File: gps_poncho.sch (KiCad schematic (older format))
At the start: 2 parts

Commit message: Se completa esquematico
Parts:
- removed J?: Micro_SD_Card_Det, symbol Micro_SD_Card_Det
- added D1: LED, symbol LED
- added J1: Micro_SD_Card, symbol Micro_SD_Card
- added R1: 1K, symbol R
- added U11: SE868-A, symbol SE868-A
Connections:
- net labels added: SPI_MOSI
- wire segments 51 -> 97
- no-connect marks 48 -> 65
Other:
- note removed: "Borrar si no se quiere \nconexiones entre ambos \nconectores"
- note removed: "Este diseño puede copiarse para iniciar un poncho simple. \n1) Copiar toda la carpeta "Basico" , renombrando \n la misma al nombre del poncho.\n2) Renombrar los archivos "basico.xxx" manteniendo \n las extensiones pero cambiando a un nombre \n descriptivo del poncho. Evitar acentos, espacios y \n caracteres ascii esxtendidos."
- note removed: "Luego de abrir el nuevo proyecto:\n1)Editar datos del rótulo.\n2)Editar los archivos del subdirectorio "doc".\n2.1) Agregarse en el archivo de licencia.\n2.2) Colocar info mínima del Poncho en el LEEME.txt\n2.3) Colocar info mínima en el CAMBIOS.txt"
- note removed: "http://www.proyecto-ciaa.com.ar/"
- moved on the sheet: XA101A, XA101B

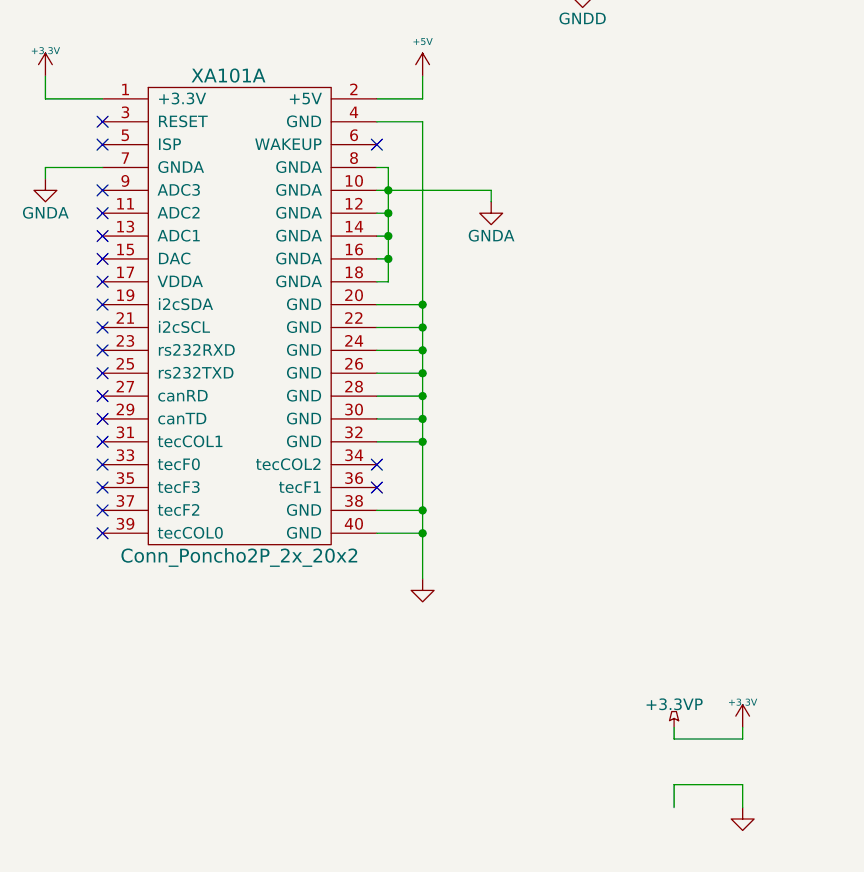
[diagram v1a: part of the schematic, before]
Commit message: Simplifico conexiones de los conectores laterales
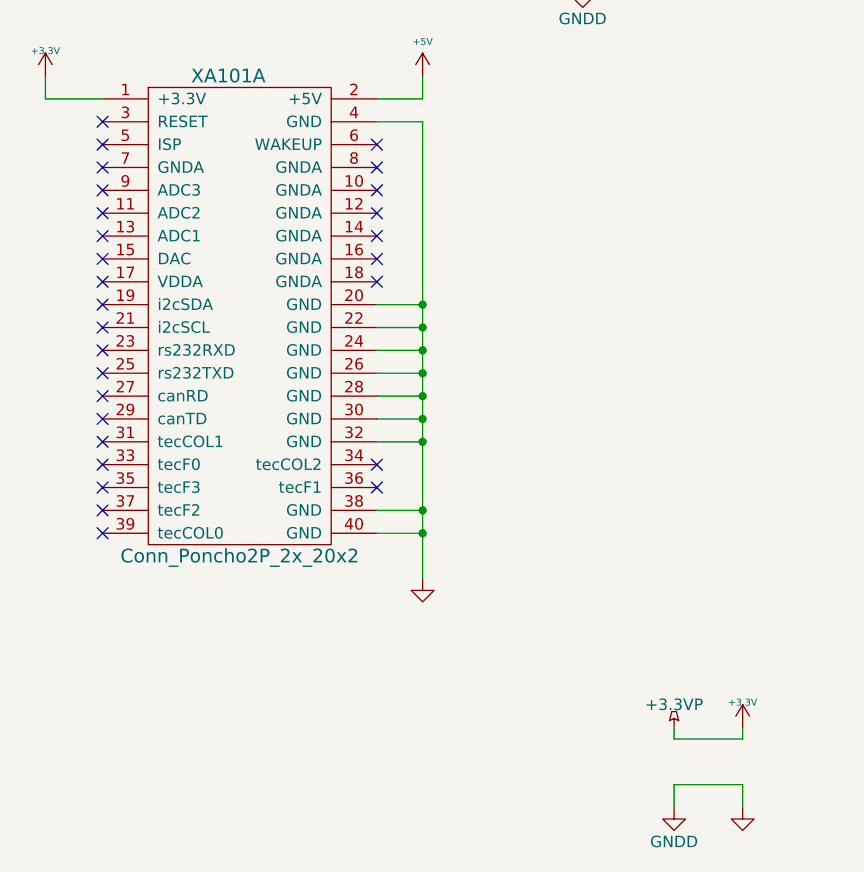
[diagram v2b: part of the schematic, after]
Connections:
- net GNDD is gone; now on net GND: D1.1 (K), J1.6 (VSS), J1.9 (SHIELD), U11.18 (RES), U11.23 (RX1), U11.24 (NC), U11.27 (NC), U11.3 (RES), U11.30 (SPI_MISO), XA101.43 (GND), XA101.45 (GND), XA101.47 (GND), XA101.51 (GND), XA101.53 (GND), XA101.57 (GND), XA101.59 (GND), XA101.65 (GND), XA101.67 (GND), XA101.77 (GND), XA101.79 (GND)
- removed net GNDA: XA101.10 (GNDA), XA101.12 (GNDA), XA101.14 (GNDA), XA101.16 (GNDA), XA101.18 (GNDA), XA101.7 (GNDA), XA101.8 (GNDA)
- no-connect marks 65 -> 72
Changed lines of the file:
@@
-$Comp
-L Conn_Poncho2P_2x_20x2 XA101
-U 1 1 57A7A0F8
-P 1700 4200
-F 0 "XA101" H 2000 4600 60  0000 C CNN
-F 1 "Conn_Poncho2P_2x_20x2" H 2050 2500 60  0000 C CNN
-F 2 "footprint:Conn_Poncho_SinBorde" H 1700 4200 60  0001 C CNN
-F 3 "" H 1700 4200 60  0000 C CNN
-F 4 "Harwin" H 1700 4200 60  0001 C CNN "Manf"
-F 5 "M50-3502042" H 1700 4200 60  0001 C CNN "Manf#"
-F 6 "952-1387-ND" H 1700 4200 60  0001 C CNN "Digikey#"
-	1    1700 4200
-	1    0    0    -1
-$EndComp
 $Comp
 L Conn_Poncho2P_2x_20x2 XA101
@@
 F 3 "" H 4250 7000 60  0000 C CNN
 	1    4250 7000
-	1    0    0    -1
-$EndComp
-$Comp
-L GNDA #PWR012
-U 1 1 57A7AE2B
-P 3150 4350
-F 0 "#PWR012" H 3150 4100 50  0001 C CNN
-F 1 "GNDA" H 3150 4200 50  0000 C CNN
-F 2 "" H 3150 4350 50  0000 C CNN
-F 3 "" H 3150 4350 50  0000 C CNN
-	1    3150 4350
-	1    0    0    -1
-$EndComp
-$Comp
-L GNDA #PWR013
-U 1 1 57A7AE5D
-P 1200 4250
-F 0 "#PWR013" H 1200 4000 50  0001 C CNN
-F 1 "GNDA" H 1200 4100 50  0000 C CNN
-F 2 "" H 1200 4250 50  0000 C CNN
-F 3 "" H 1200 4250 50  0000 C CNN
-	1    1200 4250
 	1    0    0    -1
 $EndComp
@@
 	4250 6900 4250 7000
 Wire Wire Line
-	1450 4200 1200 4200
-Wire Wire Line
-	1200 4200 1200 4250
-Wire Wire Line
-	2650 4200 2700 4200
-Wire Wire Line
-	2700 4200 2700 4700
-Wire Wire Line
-	2700 4700 2650 4700
-Wire Wire Line
-	2650 4600 2700 4600
-Connection ~ 2700 4600
-Wire Wire Line
-	2650 4500 2700 4500
-Connection ~ 2700 4500
-Wire Wire Line
-	2650 4400 2700 4400
-Connection ~ 2700 4400
-Wire Wire Line
-	2650 4300 3150 4300
-Connection ~ 2700 4300
-Wire Wire Line
-	3150 4300 3150 4350
-Wire Wire Line
 	3950 6900 4250 6900
 Wire Wire Line
@@
 	1    0    0    -1
 $EndComp
+$Comp
+L GNDD #PWR022
+U 1 1 59ED328C
+P 3950 7000
+F 0 "#PWR022" H 3950 6750 50  0001 C CNN
+F 1 "GNDD" H 3950 6850 50  0000 C CNN
+F 2 "" H 3950 7000 50  0000 C CNN
+F 3 "" H 3950 7000 50  0000 C CNN
+	1    3950 7000
+	1    0    0    -1
+$EndComp
+$Comp
+L Conn_Poncho2P_2x_20x2 XA101
+U 1 1 57A7A0F8
+P 1700 4200
+F 0 "XA101" H 2000 4600 60  0000 C CNN
+F 1 "Conn_Poncho2P_2x_20x2" H 2050 2500 60  0000 C CNN
+F 2 "footprint:Conn_Poncho_SinBorde" H 1700 4200 60  0001 C CNN
+F 3 "" H 1700 4200 60  0000 C CNN
+F 4 "Harwin" H 1700 4200 60  0001 C CNN "Manf"
+F 5 "M50-3502042" H 1700 4200 60  0001 C CNN "Manf#"
+F 6 "952-1387-ND" H 1700 4200 60  0001 C CNN "Digikey#"
+	1    1700 4200
+	1    0    0    -1
+$EndComp
+NoConn ~ 2650 4200
+NoConn ~ 2650 4300
+NoConn ~ 2650 4400
+NoConn ~ 2650 4500
+NoConn ~ 2650 4600
+NoConn ~ 2650 4700
+NoConn ~ 1450 4200
 $EndSCHEMATC

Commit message: Added datasheets: resistor and led
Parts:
- D1: value LED -> LED Green; Digikey# (none) -> 1080-1411-1-ND; Manf (none) -> Everlight Electronics Co Ltd; Manf# (none) -> QTLP630C4TR
- R1: value 1K -> 68; Digikey# (none) -> RMCF0805JT68R0TR-ND; Manf (none) -> Stackpole Electronics Inc.; Manf# (none) -> RMCF0805JT68R0
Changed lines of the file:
@@
 P 5000 5150
 F 0 "R1" V 5080 5150 50  0000 C CNN
-F 1 "1K" V 5000 5150 50  0000 C CNN
+F 1 "68" V 5000 5150 50  0000 C CNN
 F 2 "" V 4930 5150 50  0001 C CNN
 F 3 "" H 5000 5150 50  0001 C CNN
+F 4 "Stackpole Electronics Inc." V 5000 5150 60  0001 C CNN "Manf"
+F 5 "RMCF0805JT68R0" V 5000 5150 60  0001 C CNN "Manf#"
+F 6 "RMCF0805JT68R0TR-ND " V 5000 5150 60  0001 C CNN "Digikey#"
 	1    5000 5150
 	-1   0    0    1
@@
 P 5000 5550
 F 0 "D1" H 5000 5650 50  0000 C CNN
-F 1 "LED" H 5000 5450 50  0000 C CNN
+F 1 "LED Green" H 5000 5450 50  0000 C CNN
 F 2 "" H 5000 5550 50  0001 C CNN
 F 3 "" H 5000 5550 50  0001 C CNN
+F 4 "Everlight Electronics Co Ltd" H 5000 5550 60  0001 C CNN "Manf"
+F 5 "QTLP630C4TR " H 5000 5550 60  0001 C CNN "Manf#"
+F 6 "1080-1411-1-ND " H 5000 5550 60  0001 C CNN "Digikey#"
 	1    5000 5550
 	0    -1   -1   0

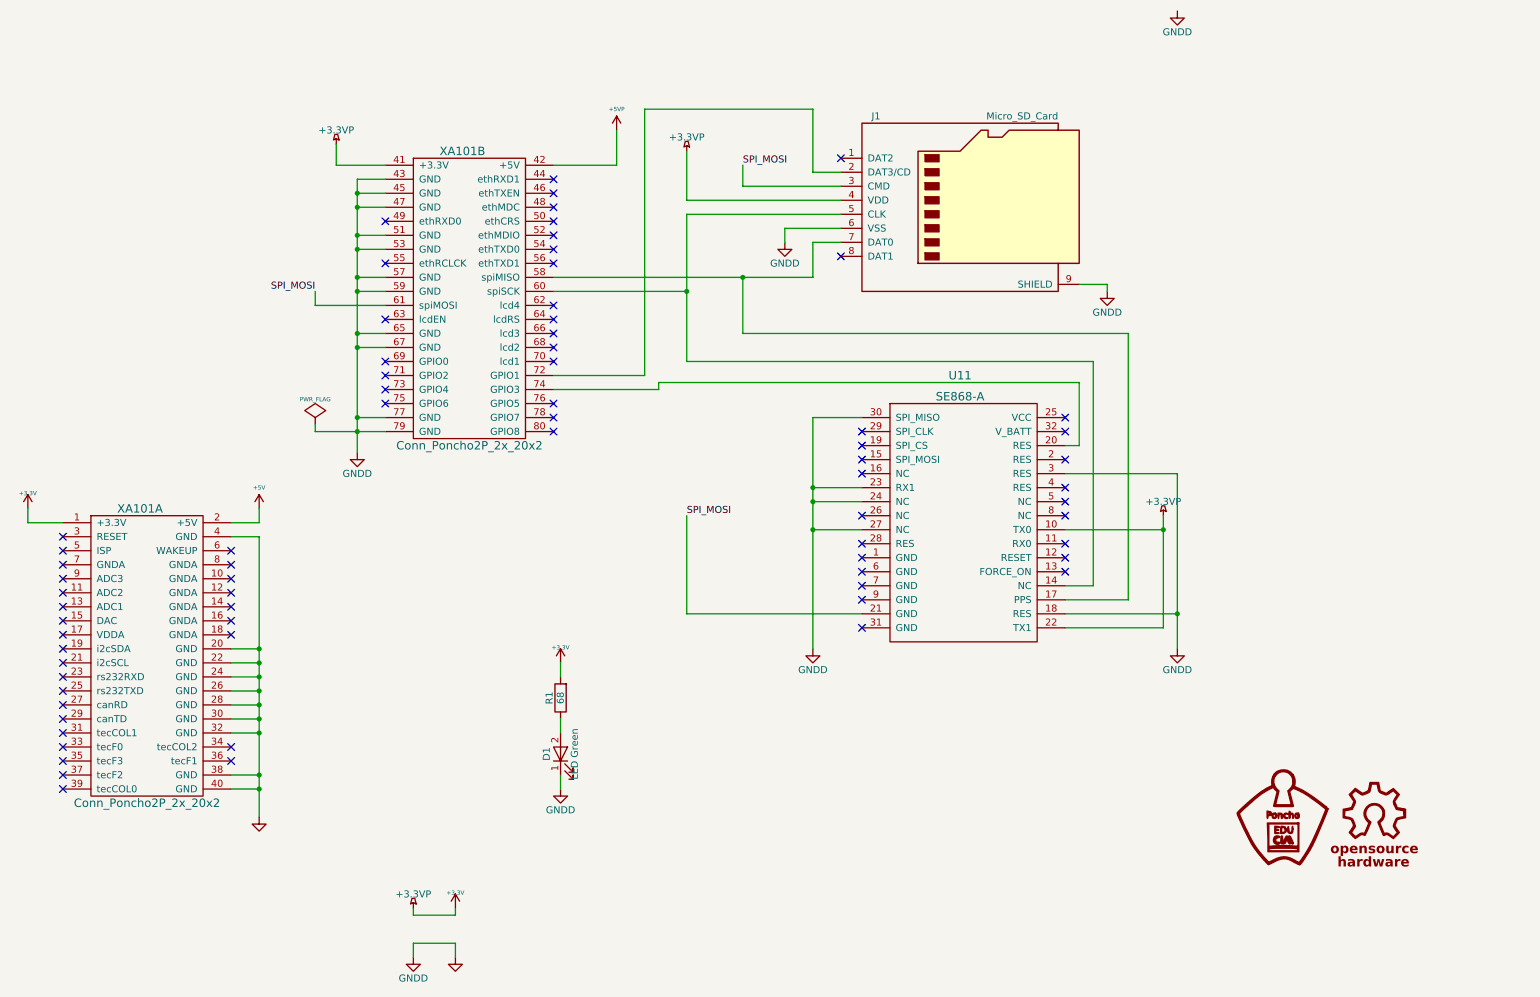
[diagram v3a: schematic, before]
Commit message: Se retiran las librerias globales exportando a la carpeta del proyecto lib/
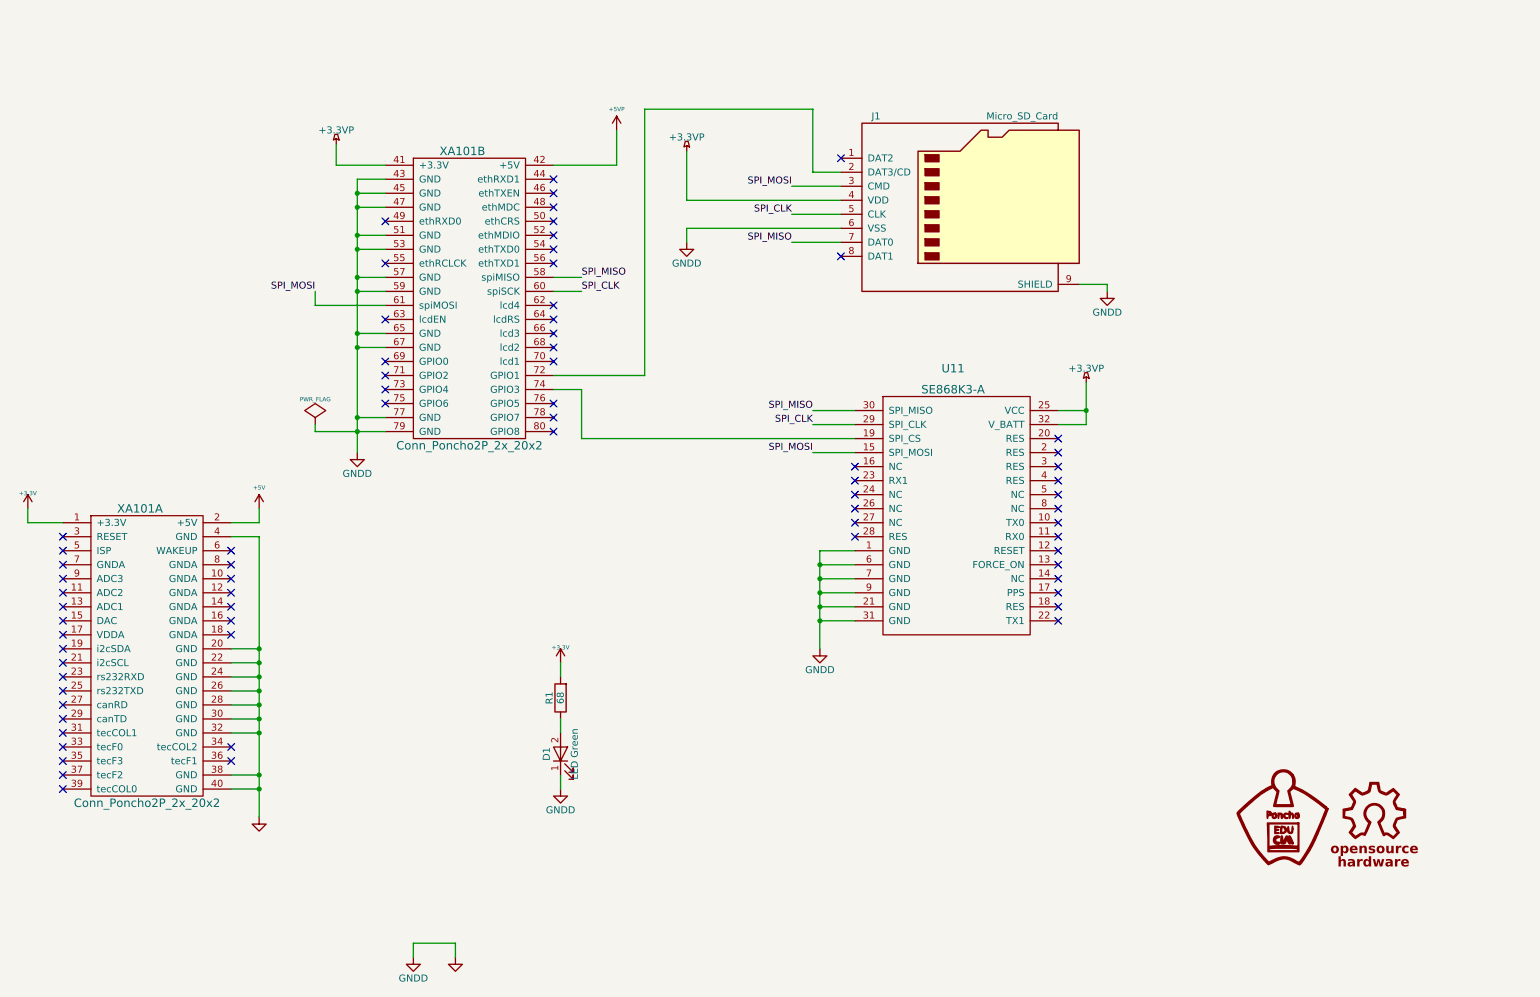
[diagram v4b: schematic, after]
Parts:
- U11: value SE868-A -> SE868K3-A; DigiKey# sd -> (none); Manf# sfdf -> SE868K3A220R001; kicost:pricing (none) -> 1:$11.71
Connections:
- net +3.3VP: now also U11.25 (VCC), U11.32 (V_BATT); no longer R1.2, U11.10 (TX0), U11.22 (TX1), XA101.1 (+3.3V)
- net GND: now also U11.1 (GND), U11.21 (GND), U11.31 (GND), U11.6 (GND), U11.7 (GND), U11.9 (GND); no longer U11.18 (RES), U11.23 (RX1), U11.24 (NC), U11.27 (NC), U11.3 (RES), U11.30 (SPI_MISO)
- net SPI_MOSI: now also U11.15 (SPI_MOSI); no longer U11.21 (GND)
- net SPI_MISO: now reaches J1.7 (DAT0), XA101.58 (spiMISO)
- net SPI_MISO: now also U11.30 (SPI_MISO); no longer U11.17 (PPS)
- net SPI_CLK: now reaches J1.5 (CLK), XA101.60 (spiSCK)
- net SPI_CLK: now also U11.29 (SPI_CLK); no longer U11.14 (NC)
- net at XA101.74 (GPIO3): now also U11.19 (SPI_CS); no longer U11.20 (RES)
- new net +3V3: R1.2, XA101.1 (+3.3V)
